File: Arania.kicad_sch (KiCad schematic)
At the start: 13 parts, among them J13 LASER, J14 GP03, J15 GP04, J16 GP04, J17 GP04, J18 GP04, J19 GP04, J20 GP04, J21 GP04, J22 GP04, J23 GP04, Q1 MMBT3904

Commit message: Finalizo el esquematico
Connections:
- net SRV18 renamed GP18
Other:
- moved on the sheet: J14, J15, J17, J18, J19, J20, J21, J22, J23

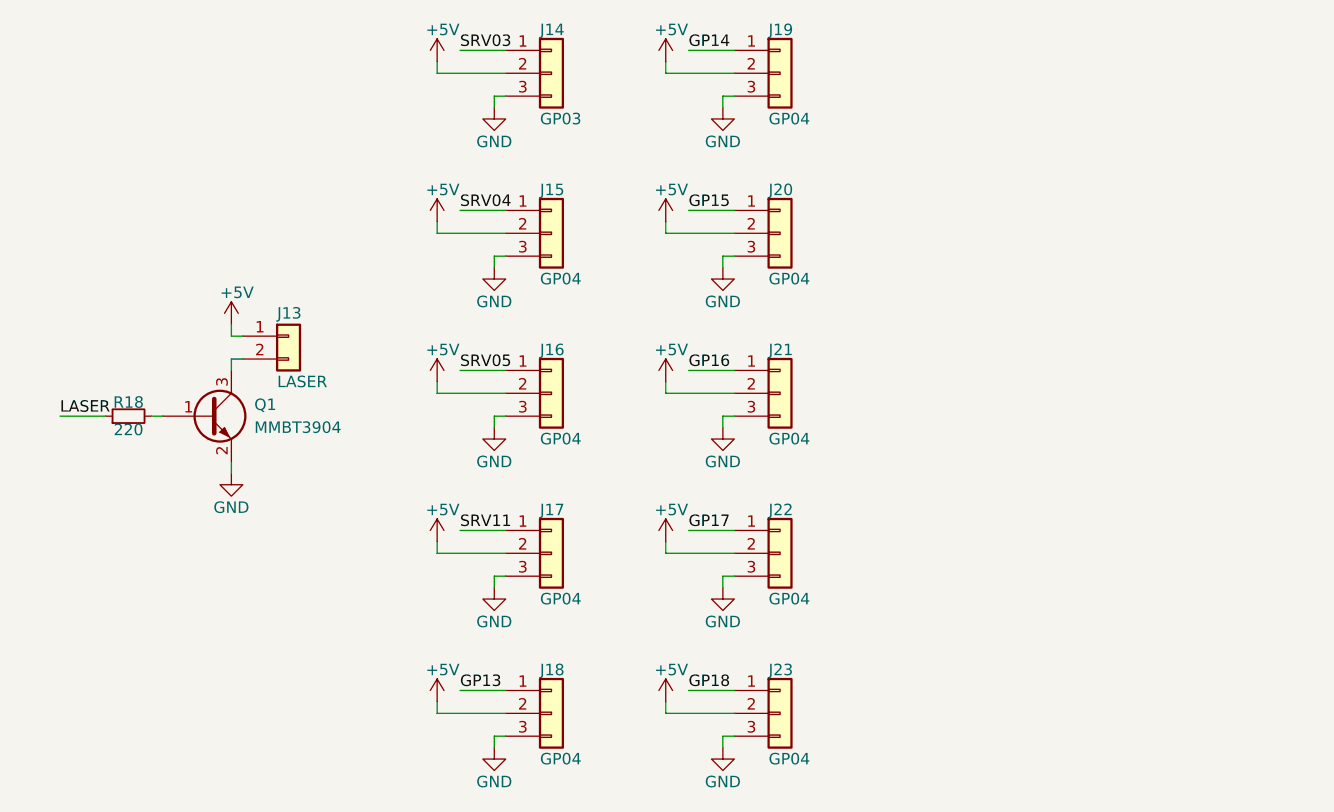
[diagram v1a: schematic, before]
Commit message: Reseteo numeracion de componentes
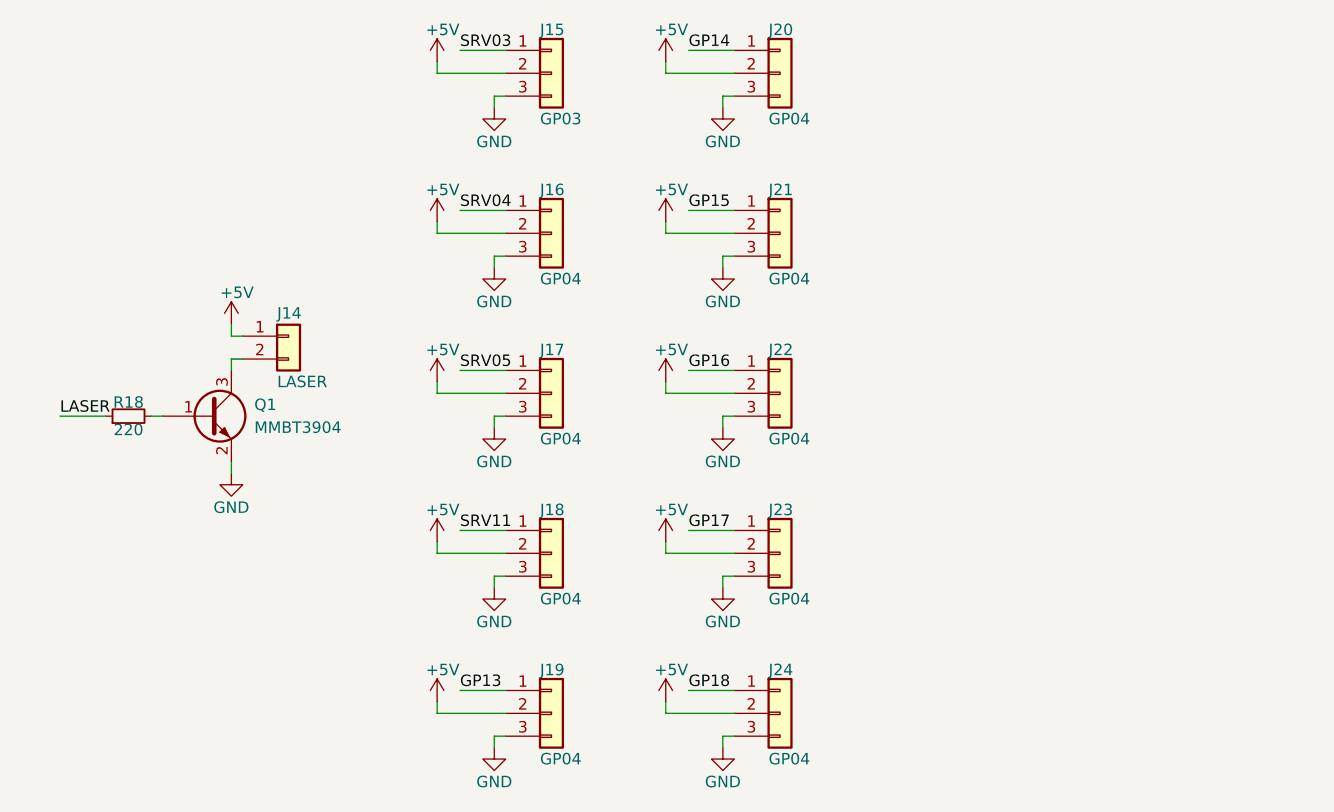
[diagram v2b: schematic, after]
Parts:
- renumbered J13 to J14, J14 to J15, J15 to J16, J16 to J17, J17 to J18, J18 to J19, J19 to J20, J20 to J21, J21 to J22, J22 to J23, J23 to J24

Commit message: Termino lista de materiales, ubico componentes e inicio ruteo
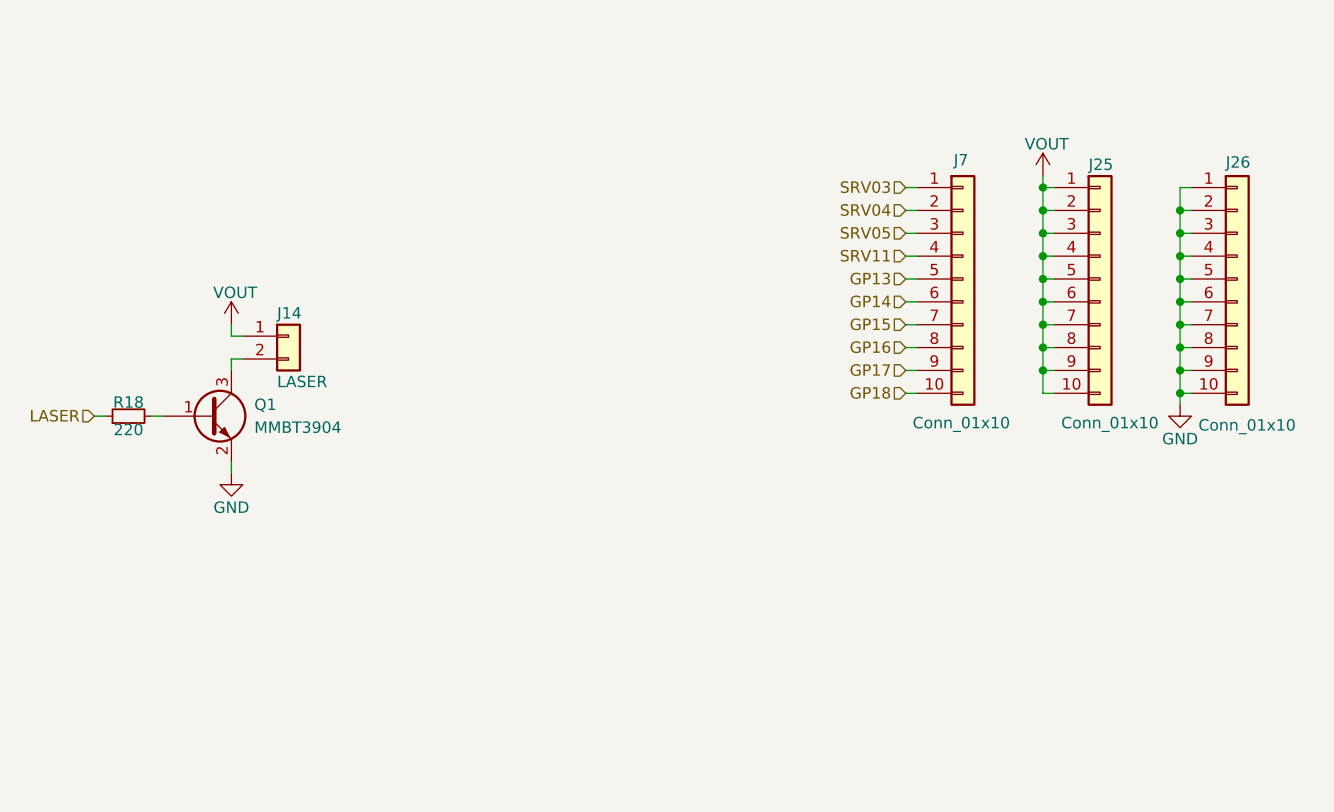
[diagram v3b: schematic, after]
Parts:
- removed J15: GP03, Connector_PinHeader_1.27mm:PinHeader_1x03_P1.27mm_Vertical, symbol Connector_Generic:Conn_01x03
- removed J16, J17, J18, J19, J20, J21, J22, J23, J24: GP04, Connector_PinHeader_1.27mm:PinHeader_1x03_P1.27mm_Vertical, symbol Connector_Generic:Conn_01x03
- added J25, J26, J7: Conn_01x10, Connector_PinHeader_2.54mm:PinHeader_1x10_P2.54mm_Vertical, symbol Connector_Generic:Conn_01x10
- J14: footprint Connector_PinHeader_1.27mm:PinHeader_1x02_P1.27mm_Vertical -> Connector_PinHeader_2.54mm:PinHeader_1x02_P2.54mm_Vertical
- Q1: PartNumber (none) -> MMBT3904; PurchaseLink (none) -> https://www.digikey.com/en/products/detail/diotec-semicondu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
- R18: PartNumber (none) -> RC0603FR-07220RL; PurchaseLink (none) -> https://www.digikey.com/en/products/detail/yageo/RC0603FR-0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
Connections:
- net GND: now also J26.1 (Pin_1), J26.10 (Pin_10), J26.2 (Pin_2), J26.3 (Pin_3), J26.4 (Pin_4), J26.5 (Pin_5), J26.6 (Pin_6), J26.7 (Pin_7), J26.8 (Pin_8), J26.9 (Pin_9)
- net GP13: now also J7.5 (Pin_5)
- net GP14: now also J7.6 (Pin_6)
- net GP15: now also J7.7 (Pin_7)
- net GP16: now also J7.8 (Pin_8)
- net GP17: now also J7.9 (Pin_9)
- net GP18: now also J7.10 (Pin_10)
- net SRV03: now also J7.1 (Pin_1)
- net SRV04: now also J7.2 (Pin_2)
- net SRV05: now also J7.3 (Pin_3)
- net SRV11: now also J7.4 (Pin_4)
- net +5V renamed VOUT
- net VOUT: now also J25.1 (Pin_1), J25.10 (Pin_10), J25.2 (Pin_2), J25.3 (Pin_3), J25.4 (Pin_4), J25.5 (Pin_5), J25.6 (Pin_6), J25.7 (Pin_7), J25.8 (Pin_8), J25.9 (Pin_9)

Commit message: Agrego capacitores y cambio footprints de borneras
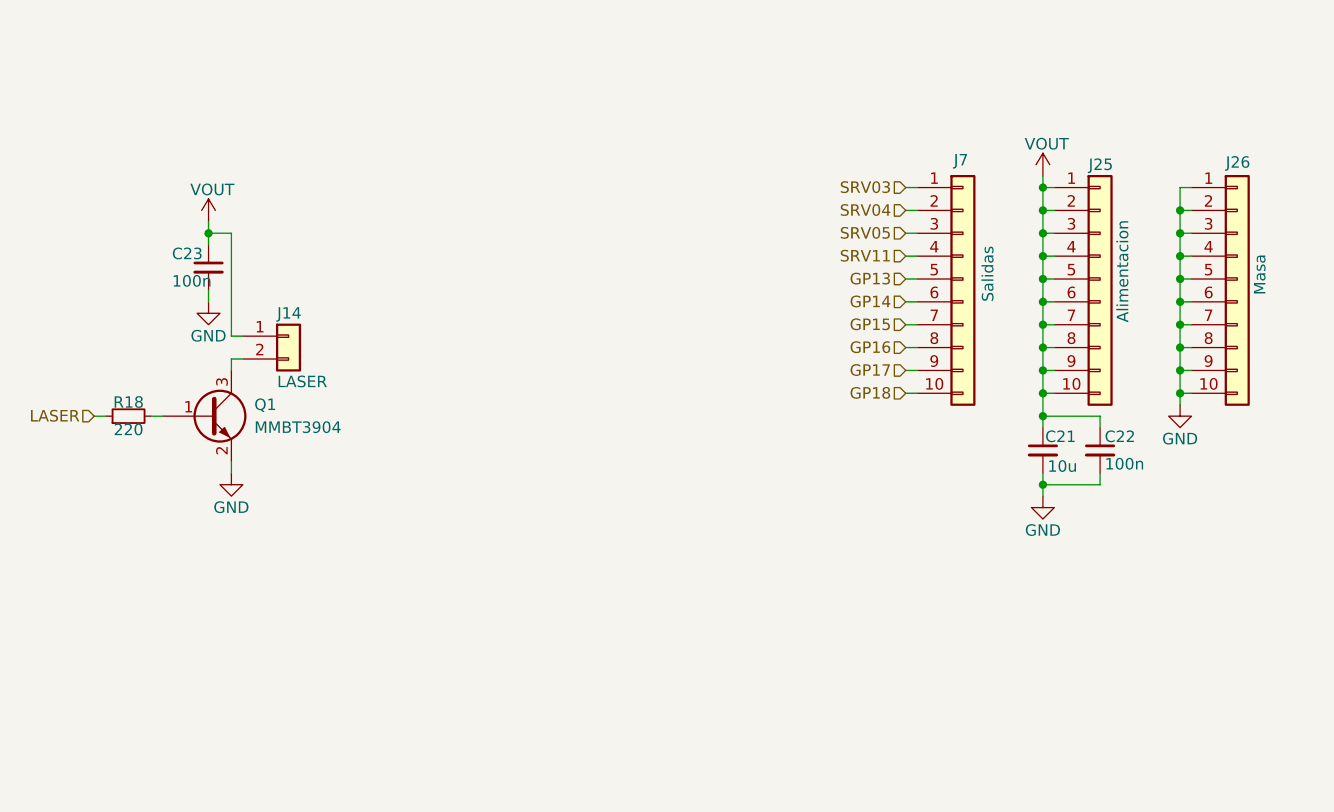
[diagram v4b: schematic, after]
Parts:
- added C21: 10u, Capacitor_SMD:C_0805_2012Metric_Pad1.18x1.45mm_HandSolder, symbol Device:C_Small
- added C22, C23: 100n, Capacitor_SMD:C_0603_1608Metric_Pad1.08x0.95mm_HandSolder, symbol Device:C_Small
- J25: value Conn_01x10 -> Alimentacion
- J26: value Conn_01x10 -> Masa
- J7: value Conn_01x10 -> Salidas
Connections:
- net GND: now also C21.2, C22.2, C23.2
- net VOUT: now also C21.1, C22.1, C23.1
